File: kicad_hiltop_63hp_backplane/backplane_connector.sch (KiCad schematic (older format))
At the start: 49 parts, among them J4 CONN_DIN_HDR_96POS, J5 CONN_DIN_HDR_96POS, J6 CONN_DIN_HDR_96POS, U3 LTC4311, U4 LTC4311

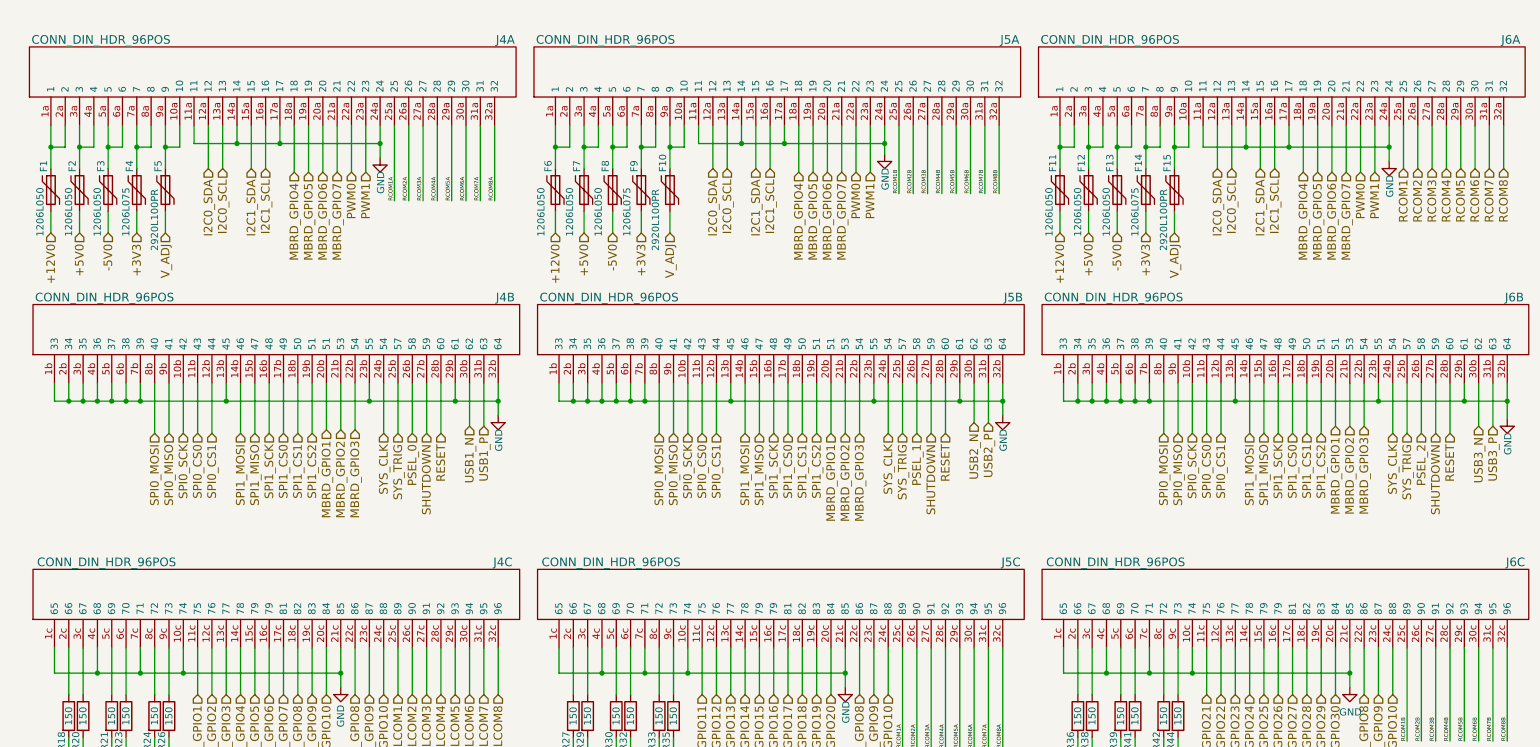
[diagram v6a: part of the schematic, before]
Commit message: schematic error reduced and footprint mapped
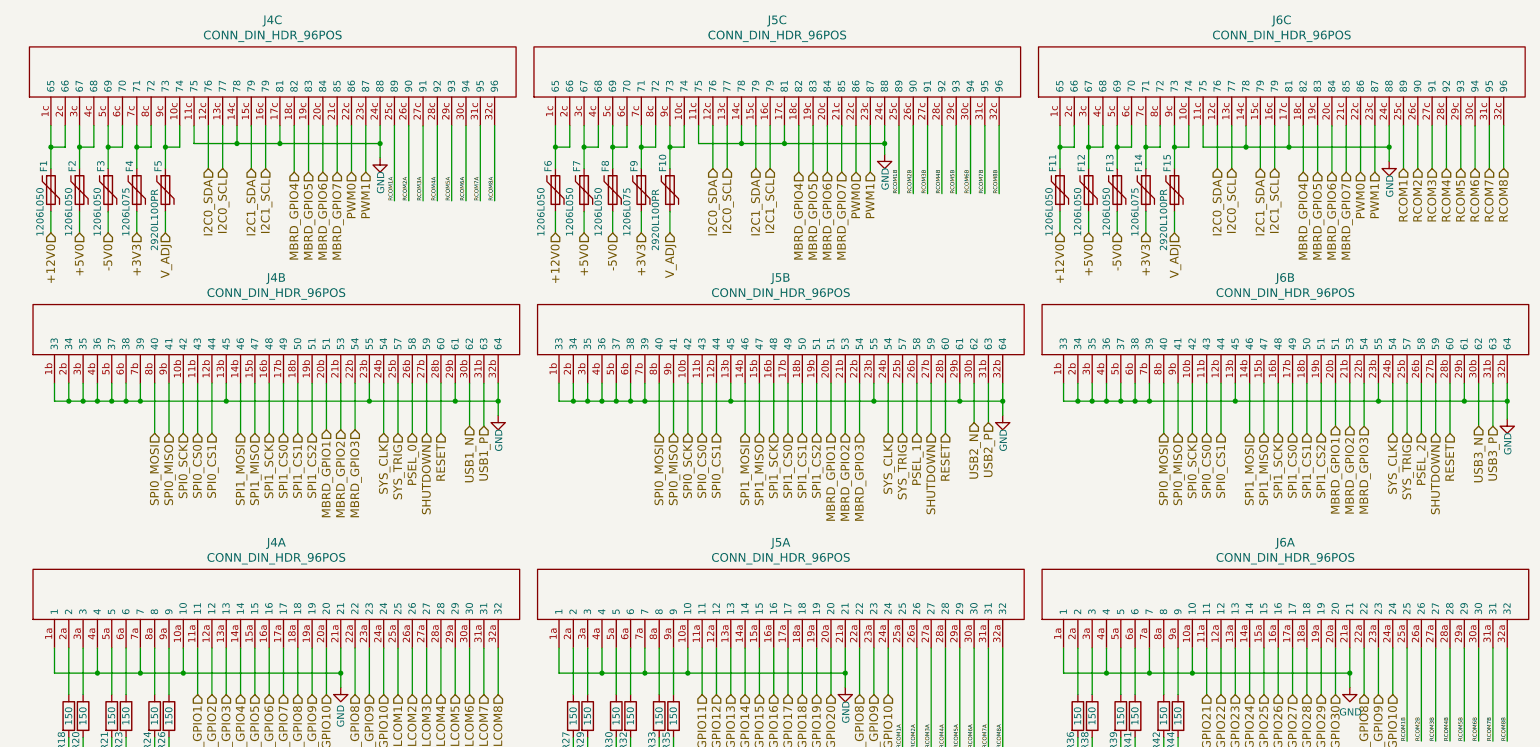
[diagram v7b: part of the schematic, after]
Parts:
- J4, J5, J6: footprint Connectors_IEC_DIN:Socket_DIN41612-CaseC1-full-Male-96Pin-3rows -> Connectors_IEC_DIN:Socket_DIN41612-CaseC1-full-Female-96Pin-3rows
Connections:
- net FPGA_GPIO1: now also J4.11a (11); no longer J4.11c (75)
- net FPGA_GPIO10: now also J4.20a (20); no longer J4.20c (84)
- net FPGA_GPIO11: now also J5.11a (11); no longer J5.11c (75)
- net FPGA_GPIO12: now also J5.12a (12); no longer J5.12c (76)
- net FPGA_GPIO13: now also J5.13a (13); no longer J5.13c (77)
- net FPGA_GPIO14: now also J5.14a (14); no longer J5.14c (78)
- net FPGA_GPIO15: now also J5.15a (15); no longer J5.15c (79)
- net FPGA_GPIO16: now also J5.16a (16); no longer J5.16c (79)
- net FPGA_GPIO17: now also J5.17a (17); no longer J5.17c (81)
- net FPGA_GPIO18: now also J5.18a (18); no longer J5.18c (82)
- net FPGA_GPIO19: now also J5.19a (19); no longer J5.19c (83)
- net FPGA_GPIO2: now also J4.12a (12); no longer J4.12c (76)
- net FPGA_GPIO20: now also J5.20a (20); no longer J5.20c (84)
- net FPGA_GPIO21: now also J6.11a (11); no longer J6.11c (75)
- net FPGA_GPIO22: now also J6.12a (12); no longer J6.12c (76)
- net FPGA_GPIO23: now also J6.13a (13); no longer J6.13c (77)
- net FPGA_GPIO24: now also J6.14a (14); no longer J6.14c (78)
- net FPGA_GPIO25: now also J6.15a (15); no longer J6.15c (79)
- net FPGA_GPIO26: now also J6.16a (16); no longer J6.16c (79)
- net FPGA_GPIO27: now also J6.17a (17); no longer J6.17c (81)
- net FPGA_GPIO28: now also J6.18a (18); no longer J6.18c (82)
- net FPGA_GPIO29: now also J6.19a (19); no longer J6.19c (83)
- net FPGA_GPIO3: now also J4.13a (13); no longer J4.13c (77)
- net FPGA_GPIO30: now also J6.20a (20); no longer J6.20c (84)
- net FPGA_GPIO4: now also J4.14a (14); no longer J4.14c (78)
- net FPGA_GPIO5: now also J4.15a (15); no longer J4.15c (79)
- net FPGA_GPIO6: now also J4.16a (16); no longer J4.16c (79)
- net FPGA_GPIO7: now also J4.17a (17); no longer J4.17c (81)
- net FPGA_GPIO8: now also J4.18a (18); no longer J4.18c (82)
- net FPGA_GPIO9: now also J4.19a (19); no longer J4.19c (83)
- net GND: now also J4.10a (10), J4.11c (75), J4.14c (78), J4.17c (81), J4.1a (1), J4.21a (21), J4.24c (88), J4.4a (4), J4.7a (7), J5.10a (10), J5.11c (75), J5.14c (78), J5.17c (81), J5.1a (1), J5.21a (21), J5.24c (88), J5.4a (4), J5.7a (7), J6.10a (10), J6.11c (75), J6.14c (78), J6.17c (81), J6.1a (1), J6.21a (21), J6.24c (88), J6.4a (4), J6.7a (7); no longer J4.10c (74), J4.11a (11), J4.14a (14), J4.17a (17), J4.1c (65), J4.21c (85), J4.24a (24), J4.4c (68), J4.7c (71), J5.10c (74), J5.11a (11), J5.14a (14), J5.17a (17), J5.1c (65), J5.21c (85), J5.24a (24), J5.4c (68), J5.7c (71), J6.10c (74), J6.11a (11), J6.14a (14), J6.17a (17), J6.1c (65), J6.21c (85), J6.24a (24), J6.4c (68), J6.7c (71)
- net I2C0_SCL: now also J4.13c (77), J5.13c (77), J6.13c (77); no longer J4.13a (13), J5.13a (13), J6.13a (13)
- net I2C0_SDA: now also J4.12c (76), J5.12c (76), J6.12c (76); no longer J4.12a (12), J5.12a (12), J6.12a (12)
- net I2C1_SCL: now also J4.16c (79), J5.16c (79), J6.16c (79); no longer J4.16a (16), J5.16a (16), J6.16a (16)
- net I2C1_SDA: now also J4.15c (79), J5.15c (79), J6.15c (79); no longer J4.15a (15), J5.15a (15), J6.15a (15)
- net LCOM1: now also J4.25a (25); no longer J4.25c (89)
- net LCOM2: now also J4.26a (26); no longer J4.26c (90)
- net LCOM3: now also J4.27a (27); no longer J4.27c (91)
- net LCOM4: now also J4.28a (28); no longer J4.28c (92)
- net LCOM5: now also J4.29a (29); no longer J4.29c (93)
- net LCOM6: now also J4.30a (30); no longer J4.30c (94)
- net LCOM7: now also J4.31a (31); no longer J4.31c (95)
- net LCOM8: now also J4.32a (32); no longer J4.32c (96)
- net MBRD_GPIO10: now also J4.24a (24), J5.24a (24), J6.24a (24); no longer J4.24c (88), J5.24c (88), J6.24c (88)
- net MBRD_GPIO4: now also J4.18c (82), J5.18c (82), J6.18c (82); no longer J4.18a (18), J5.18a (18), J6.18a (18)
- net MBRD_GPIO5: now also J4.19c (83), J5.19c (83), J6.19c (83); no longer J4.19a (19), J5.19a (19), J6.19a (19)
- net MBRD_GPIO6: now also J4.20c (84), J5.20c (84), J6.20c (84); no longer J4.20a (20), J5.20a (20), J6.20a (20)
- net MBRD_GPIO7: now also J4.21c (85), J5.21c (85), J6.21c (85); no longer J4.21a (21), J5.21a (21), J6.21a (21)
- net MBRD_GPIO8: now also J4.22a (22), J5.22a (22), J6.22a (22); no longer J4.22c (86), J5.22c (86), J6.22c (86)
- net MBRD_GPIO9: now also J4.23a (23), J5.23a (23), J6.23a (23); no longer J4.23c (87), J5.23c (87), J6.23c (87)
- net PWM0: now also J4.22c (86), J5.22c (86), J6.22c (86); no longer J4.22a (22), J5.22a (22), J6.22a (22)
- net PWM1: now also J4.23c (87), J5.23c (87), J6.23c (87); no longer J4.23a (23), J5.23a (23), J6.23a (23)
- net RCOM1: now also J6.25c (89); no longer J6.25a (25)
- net RCOM1A: now also J4.25c (89), J5.25a (25); no longer J4.25a (25), J5.25c (89)
- net RCOM1B: now also J5.25c (89), J6.25a (25); no longer J5.25a (25), J6.25c (89)
- net RCOM2: now also J6.26c (90); no longer J6.26a (26)
- net RCOM2A: now also J4.26c (90), J5.26a (26); no longer J4.26a (26), J5.26c (90)
- net RCOM2B: now also J5.26c (90), J6.26a (26); no longer J5.26a (26), J6.26c (90)
- net RCOM3: now also J6.27c (91); no longer J6.27a (27)
- net RCOM3A: now also J4.27c (91), J5.27a (27); no longer J4.27a (27), J5.27c (91)
- net RCOM3B: now also J5.27c (91), J6.27a (27); no longer J5.27a (27), J6.27c (91)
- net RCOM4: now also J6.28c (92); no longer J6.28a (28)
- net RCOM4A: now also J4.28c (92), J5.28a (28); no longer J4.28a (28), J5.28c (92)
- net RCOM4B: now also J5.28c (92), J6.28a (28); no longer J5.28a (28), J6.28c (92)
- net RCOM5: now also J6.29c (93); no longer J6.29a (29)
- net RCOM5A: now also J4.29c (93), J5.29a (29); no longer J4.29a (29), J5.29c (93)
- net RCOM5B: now also J5.29c (93), J6.29a (29); no longer J5.29a (29), J6.29c (93)
- net RCOM6: now also J6.30c (94); no longer J6.30a (30)
- net RCOM6A: now also J4.30c (94), J5.30a (30); no longer J4.30a (30), J5.30c (94)
- net RCOM6B: now also J5.30c (94), J6.30a (30); no longer J5.30a (30), J6.30c (94)
- net RCOM7: now also J6.31c (95); no longer J6.31a (31)
- net RCOM7A: now also J4.31c (95), J5.31a (31); no longer J4.31a (31), J5.31c (95)
- net RCOM7B: now also J5.31c (95), J6.31a (31); no longer J5.31a (31), J6.31c (95)
- net RCOM8: now also J6.32c (96); no longer J6.32a (32)
- net RCOM8A: now also J4.32c (96), J5.32a (32); no longer J4.32a (32), J5.32c (96)
- net RCOM8B: now also J5.32c (96), J6.32a (32); no longer J5.32a (32), J6.32c (96)
- net at R21.1: now also J4.5a (5); no longer J4.5c (69)
- net at R23.1: now also J4.6a (6); no longer J4.6c (70)
- net at R30.1: now also J5.5a (5); no longer J5.5c (69)
- net at R32.1: now also J5.6a (6); no longer J5.6c (70)
- net at R24.1: now also J4.8a (8); no longer J4.8c (72)
- net at R26.1: now also J4.9a (9); no longer J4.9c (73)
- net at R33.1: now also J5.8a (8); no longer J5.8c (72)
- net at R35.1: now also J5.9a (9); no longer J5.9c (73)
- net at R39.1: now also J6.5a (5); no longer J6.5c (69)
- net at R41.1: now also J6.6a (6); no longer J6.6c (70)
- net at R42.1: now also J6.8a (8); no longer J6.8c (72)
- net at R44.1: now also J6.9a (9); no longer J6.9c (73)
- net at R18.1: now also J4.2a (2); no longer J4.2c (66)
- net at R20.1: now also J4.3a (3); no longer J4.3c (67)
- net at R36.1: now also J6.2a (2); no longer J6.2c (66)
- net at R38.1: now also J6.3a (3); no longer J6.3c (67)
- net at R27.1: now also J5.2a (2); no longer J5.2c (66)
- net at R29.1: now also J5.3a (3); no longer J5.3c (67)
- new net: F5.1, J4.10c (74), J4.9c (73)
- new net: F1.1, J4.1c (65), J4.2c (66)
- new net: F2.1, J4.3c (67), J4.4c (68)
- new net: F3.1, J4.5c (69), J4.6c (70)
- new net: F4.1, J4.7c (71), J4.8c (72)
- new net: F10.1, J5.10c (74), J5.9c (73)
- new net: F6.1, J5.1c (65), J5.2c (66)
- new net: F7.1, J5.3c (67), J5.4c (68)
- new net: F8.1, J5.5c (69), J5.6c (70)
- new net: F9.1, J5.7c (71), J5.8c (72)
- new net: F15.1, J6.10c (74), J6.9c (73)
- new net: F11.1, J6.1c (65), J6.2c (66)
- new net: F12.1, J6.3c (67), J6.4c (68)
- new net: F13.1, J6.5c (69), J6.6c (70)
- new net: F14.1, J6.7c (71), J6.8c (72)
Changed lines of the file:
@@
 Wire Wire Line
 	4725 5950 4725 5900
-$Comp
-L gti_Lattice:CONN_DIN_HDR_96POS J6
-U 3 1 5CF33CB5
-P 7700 4275
-F 0 "J6" V 7750 900 60  0000 L CNN
-F 1 "CONN_DIN_HDR_96POS" V 7750 3275 60  0000 L CNN
-F 2 "Connectors_IEC_DIN:Socket_DIN41612-CaseC1-full-Male-96Pin-3rows" H 7500 4225 60  0001 C CNN
-F 3 "" H 7500 4225 60  0001 C CNN
-	3    7700 4275
-	0    -1   -1   0
-$EndComp
-$Comp
-L gti_Lattice:CONN_DIN_HDR_96POS J5
-U 3 1 5CF3408F
-P 4175 4275
-F 0 "J5" V 4225 900 60  0000 L CNN
-F 1 "CONN_DIN_HDR_96POS" V 4225 3275 60  0000 L CNN
-F 2 "Connectors_IEC_DIN:Socket_DIN41612-CaseC1-full-Male-96Pin-3rows" H 3975 4225 60  0001 C CNN
-F 3 "" H 3975 4225 60  0001 C CNN
-	3    4175 4275
-	0    -1   -1   0
-$EndComp
-$Comp
-L gti_Lattice:CONN_DIN_HDR_96POS J4
-U 3 1 5CF345E0
-P 650 4275
-F 0 "J4" V 700 925 60  0000 L CNN
-F 1 "CONN_DIN_HDR_96POS" V 700 3275 60  0000 L CNN
-F 2 "Connectors_IEC_DIN:Socket_DIN41612-CaseC1-full-Male-96Pin-3rows" H 450 4225 60  0001 C CNN
-F 3 "" H 450 4225 60  0001 C CNN
-	3    650  4275
-	0    -1   -1   0
-$EndComp
 Wire Wire Line
 	800  2975 800  3100
@@
 Text HLabel 6125 3325 3    60   Input ~ 0
 SPI1_CS2
-$Comp
-L gti_Lattice:CONN_DIN_HDR_96POS J4
-U 2 1 5C2DCD4F
-P 650 2425
-F 0 "J4" V 700 -875 60  0000 C CNN
-F 1 "CONN_DIN_HDR_96POS" V 700 1925 60  0000 C CNN
-F 2 "Connectors_IEC_DIN:Socket_DIN41612-CaseC1-full-Male-96Pin-3rows" H 450 2375 60  0001 C CNN
-F 3 "" H 450 2375 60  0001 C CNN
-	2    650  2425
-	0    -1   -1   0
-$EndComp
-$Comp
-L gti_Lattice:CONN_DIN_HDR_96POS J5
-U 2 1 5C2DD334
-P 4175 2425
-F 0 "J5" V 4225 -900 60  0000 C CNN
-F 1 "CONN_DIN_HDR_96POS" V 4225 1925 60  0000 C CNN
-F 2 "Connectors_IEC_DIN:Socket_DIN41612-CaseC1-full-Male-96Pin-3rows" H 3975 2375 60  0001 C CNN
-F 3 "" H 3975 2375 60  0001 C CNN
-	2    4175 2425
-	0    -1   -1   0
-$EndComp
-$Comp
-L gti_Lattice:CONN_DIN_HDR_96POS J6
-U 2 1 5C2DD5A4
-P 7700 2425
-F 0 "J6" V 7750 -875 60  0000 C CNN
-F 1 "CONN_DIN_HDR_96POS" V 7750 1925 60  0000 C CNN
-F 2 "Connectors_IEC_DIN:Socket_DIN41612-CaseC1-full-Male-96Pin-3rows" H 7500 2375 60  0001 C CNN
-F 3 "" H 7500 2375 60  0001 C CNN
-	2    7700 2425
-	0    -1   -1   0
-$EndComp
-$Comp
-L gti_Lattice:CONN_DIN_HDR_96POS J6
-U 1 1 5C2DD941
-P 7675 625
-F 0 "J6" V 7725 -2675 60  0000 C CNN
-F 1 "CONN_DIN_HDR_96POS" V 7725 125 60  0000 C CNN
-F 2 "Connectors_IEC_DIN:Socket_DIN41612-CaseC1-full-Male-96Pin-3rows" H 7475 575 60  0001 C CNN
-F 3 "" H 7475 575 60  0001 C CNN
-	1    7675 625
-	0    -1   -1   0
-$EndComp
-$Comp
-L gti_Lattice:CONN_DIN_HDR_96POS J5
-U 1 1 5C2DDD3E
-P 4150 625
-F 0 "J5" V 4200 -2700 60  0000 C CNN
-F 1 "CONN_DIN_HDR_96POS" V 4200 125 60  0000 C CNN
-F 2 "Connectors_IEC_DIN:Socket_DIN41612-CaseC1-full-Male-96Pin-3rows" H 3950 575 60  0001 C CNN
-F 3 "" H 3950 575 60  0001 C CNN
-	1    4150 625
-	0    -1   -1   0
-$EndComp
-$Comp
-L gti_Lattice:CONN_DIN_HDR_96POS J4
-U 1 1 5C2DE0D8
-P 625 625
-F 0 "J4" V 675 -2700 60  0000 C CNN
-F 1 "CONN_DIN_HDR_96POS" V 675 125 60  0000 C CNN
-F 2 "Connectors_IEC_DIN:Socket_DIN41612-CaseC1-full-Male-96Pin-3rows" H 425 575 60  0001 C CNN
-F 3 "" H 425 575 60  0001 C CNN
-	1    625  625
-	0    -1   -1   0
-$EndComp
 Text HLabel 3575 7025 0    39   Input ~ 0
 +3V3
@@
 Wire Wire Line
 	10750 2975 10750 3275
+$Comp
+L gti_Lattice:CONN_DIN_HDR_96POS J4
+U 1 1 5C446251
+P 650 4275
+F 0 "J4" V 837 2575 60  0000 C CNN
+F 1 "CONN_DIN_HDR_96POS" V 731 2575 60  0000 C CNN
+F 2 "Connectors_IEC_DIN:Socket_DIN41612-CaseC1-full-Female-96Pin-3rows" H 450 4225 60  0001 C CNN
+F 3 "" H 450 4225 60  0001 C CNN
+	1    650  4275
+	0    -1   -1   0
+$EndComp
+$Comp
+L gti_Lattice:CONN_DIN_HDR_96POS J5
+U 1 1 5C4466C1
+P 4175 4275
+F 0 "J5" V 4362 2575 60  0000 C CNN
+F 1 "CONN_DIN_HDR_96POS" V 4256 2575 60  0000 C CNN
+F 2 "Connectors_IEC_DIN:Socket_DIN41612-CaseC1-full-Female-96Pin-3rows" H 3975 4225 60  0001 C CNN
+F 3 "" H 3975 4225 60  0001 C CNN
+	1    4175 4275
+	0    -1   -1   0
+$EndComp
+$Comp
+L gti_Lattice:CONN_DIN_HDR_96POS J6
+U 1 1 5C446ABA
+P 7700 4275
+F 0 "J6" V 7887 2575 60  0000 C CNN
+F 1 "CONN_DIN_HDR_96POS" V 7781 2575 60  0000 C CNN
+F 2 "Connectors_IEC_DIN:Socket_DIN41612-CaseC1-full-Female-96Pin-3rows" H 7500 4225 60  0001 C CNN
+F 3 "" H 7500 4225 60  0001 C CNN
+	1    7700 4275
+	0    -1   -1   0
+$EndComp
+$Comp
+L gti_Lattice:CONN_DIN_HDR_96POS J4
+U 2 1 5C446E37
+P 650 2425
+F 0 "J4" V 837 725 60  0000 C CNN
+F 1 "CONN_DIN_HDR_96POS" V 731 725 60  0000 C CNN
+F 2 "Connectors_IEC_DIN:Socket_DIN41612-CaseC1-full-Female-96Pin-3rows" H 450 2375 60  0001 C CNN
+F 3 "" H 450 2375 60  0001 C CNN
+	2    650  2425
+	0    -1   -1   0
+$EndComp
+$Comp
+L gti_Lattice:CONN_DIN_HDR_96POS J5
+U 2 1 5C4471B0
+P 4175 2425
+F 0 "J5" V 4362 725 60  0000 C CNN
+F 1 "CONN_DIN_HDR_96POS" V 4256 725 60  0000 C CNN
+F 2 "Connectors_IEC_DIN:Socket_DIN41612-CaseC1-full-Female-96Pin-3rows" H 3975 2375 60  0001 C CNN
+F 3 "" H 3975 2375 60  0001 C CNN
+	2    4175 2425
+	0    -1   -1   0
+$EndComp
+$Comp
+L gti_Lattice:CONN_DIN_HDR_96POS J6
+U 2 1 5C44765E
+P 7700 2425
+F 0 "J6" V 7887 725 60  0000 C CNN
+F 1 "CONN_DIN_HDR_96POS" V 7781 725 60  0000 C CNN
+F 2 "Connectors_IEC_DIN:Socket_DIN41612-CaseC1-full-Female-96Pin-3rows" H 7500 2375 60  0001 C CNN
+F 3 "" H 7500 2375 60  0001 C CNN
+	2    7700 2425
+	0    -1   -1   0
+$EndComp
+$Comp
+L gti_Lattice:CONN_DIN_HDR_96POS J4
+U 3 1 5C447924
+P 625 625
+F 0 "J4" V 812 -1075 60  0000 C CNN
+F 1 "CONN_DIN_HDR_96POS" V 706 -1075 60  0000 C CNN
+F 2 "Connectors_IEC_DIN:Socket_DIN41612-CaseC1-full-Female-96Pin-3rows" H 425 575 60  0001 C CNN
+F 3 "" H 425 575 60  0001 C CNN
+	3    625  625
+	0    -1   -1   0
+$EndComp
+$Comp
+L gti_Lattice:CONN_DIN_HDR_96POS J5
+U 3 1 5C447CEB
+P 4150 625
+F 0 "J5" V 4337 -1075 60  0000 C CNN
+F 1 "CONN_DIN_HDR_96POS" V 4231 -1075 60  0000 C CNN
+F 2 "Connectors_IEC_DIN:Socket_DIN41612-CaseC1-full-Female-96Pin-3rows" H 3950 575 60  0001 C CNN
+F 3 "" H 3950 575 60  0001 C CNN
+	3    4150 625
+	0    -1   -1   0
+$EndComp
+$Comp
+L gti_Lattice:CONN_DIN_HDR_96POS J6
+U 3 1 5C447F84
+P 7675 625
+F 0 "J6" V 7862 -1075 60  0000 C CNN
+F 1 "CONN_DIN_HDR_96POS" V 7756 -1075 60  0000 C CNN
+F 2 "Connectors_IEC_DIN:Socket_DIN41612-CaseC1-full-Female-96Pin-3rows" H 7475 575 60  0001 C CNN
+F 3 "" H 7475 575 60  0001 C CNN
+	3    7675 625
+	0    -1   -1   0
+$EndComp
 $EndSCHEMATC

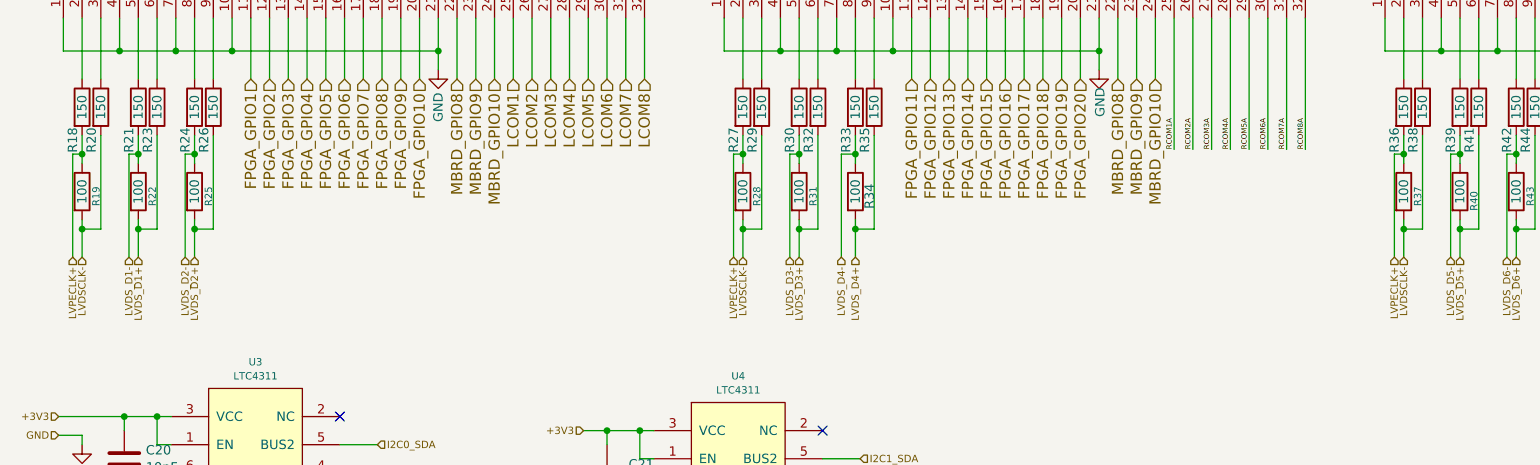
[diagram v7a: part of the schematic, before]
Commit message: pci connector connection moved to bottom layer, FTDI routing and FPGA power routing
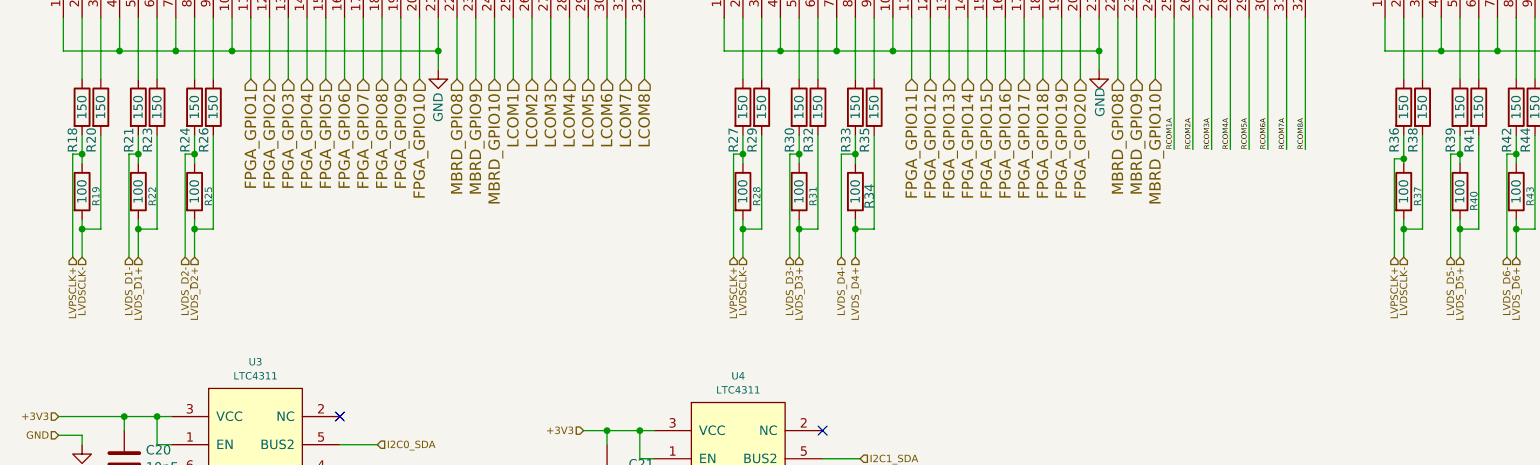
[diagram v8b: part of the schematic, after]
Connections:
- net LVPECLK+ renamed LVPSCLK+
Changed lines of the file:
@@
 LVDS_D1+
 Text HLabel 850  6100 3    39   Input ~ 0
-LVPECLK+
+LVPSCLK+
 Text HLabel 900  6100 3    39   Input ~ 0
 LVDSCLK-
@@
 Connection ~ 4425 5550
 Text HLabel 4375 6100 3    39   Input ~ 0
-LVPECLK+
+LVPSCLK+
 Text HLabel 4425 6100 3    39   Input ~ 0
 LVDSCLK-
@@
 $EndComp
 Wire Wire Line
-	7950 5600 7950 5550
-Wire Wire Line
 	8050 5450 8050 5950
 Wire Wire Line
@@
 	7950 6100 7950 5950
 Connection ~ 7950 5950
-Wire Wire Line
-	7900 6100 7900 5550
-Wire Wire Line
-	7900 5550 7950 5550
-Connection ~ 7950 5550
 Text HLabel 7900 6100 3    39   Input ~ 0
-LVPECLK+
+LVPSCLK+
 Text HLabel 7950 6100 3    39   Input ~ 0
 LVDSCLK-
 Wire Wire Line
 	7950 5950 7950 5900
-Wire Wire Line
-	7950 5550 7950 5450
 $Comp
 L device:Polyfuse F1
@@
 	0    -1   -1   0
 $EndComp
+Wire Wire Line
+	7950 5450 7950 5575
+Wire Wire Line
+	7900 6100 7900 5575
+Wire Wire Line
+	7900 5575 7950 5575
+Connection ~ 7950 5575
+Wire Wire Line
+	7950 5575 7950 5600
 $EndSCHEMATC
